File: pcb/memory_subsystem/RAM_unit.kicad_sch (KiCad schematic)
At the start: 6 parts, among them U3 74LS245

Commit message: Tracks finished
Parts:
- C1, C2, C3: footprint Capacitor_SMD:C_0805_2012Metric -> Capacitor_SMD:C_0805_2012Metric_Pad1.18x1.45mm_HandSolder
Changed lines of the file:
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@@
 			)
 		)
-		(property "Footprint" "Capacitor_SMD:C_0805_2012Metric"
+		(property "Footprint" "Capacitor_SMD:C_0805_2012Metric_Pad1.18x1.45mm_HandSolder"
 			(at 187.96 88.5952 0)
 			(hide yes)
@@
 			)
 		)
-		(property "Footprint" "Capacitor_SMD:C_0805_2012Metric"
+		(property "Footprint" "Capacitor_SMD:C_0805_2012Metric_Pad1.18x1.45mm_HandSolder"
 			(at 149.86 47.9552 0)
 			(hide yes)
@@
 			)
 		)
-		(property "Footprint" "Capacitor_SMD:C_0805_2012Metric"
+		(property "Footprint" "Capacitor_SMD:C_0805_2012Metric_Pad1.18x1.45mm_HandSolder"
 			(at 78.74 47.9552 0)
 			(hide yes)

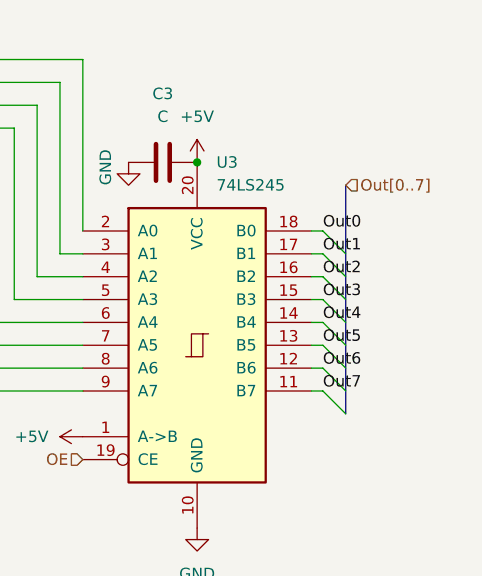
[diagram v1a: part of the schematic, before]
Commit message: Finished mem subsystem pcb
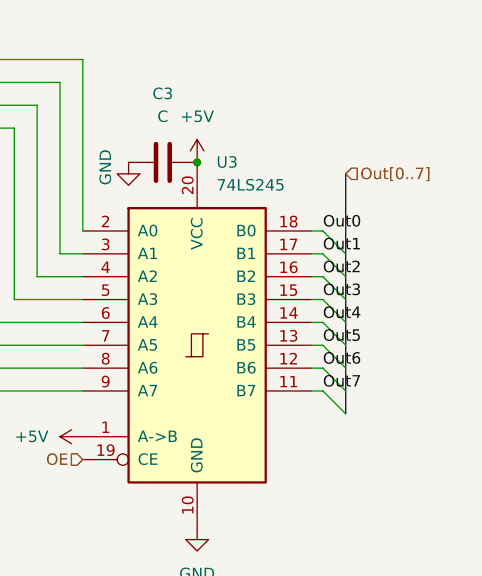
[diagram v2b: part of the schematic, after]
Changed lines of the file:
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@@
 	(bus
 		(pts
-			(xy 212.09 90.17) (xy 212.09 115.57)
+			(xy 212.09 88.9) (xy 212.09 115.57)
 		)
 		(stroke
@@
 	(hierarchical_label "Out[0..7]"
 		(shape input)
-		(at 212.09 90.17 0)
+		(at 212.09 88.9 0)
 		(effects
 			(font
@@
 					(unit 1)
 				)
+				(path "/eef9c2f8-b48e-448a-907d-9c9f187d4399/42f51e2d-d8b6-4a94-b1a8-da7d5a86e9c8"
+					(reference "#PWR038")
+					(unit 1)
+				)
 				(path "/eef9c2f8-b48e-448a-907d-9c9f187d4399/7681efea-75da-45e2-a65e-85a008f87d4d"
 					(reference "#PWR019")
-					(unit 1)
-				)
-				(path "/eef9c2f8-b48e-448a-907d-9c9f187d4399/ed633529-ad37-432a-9a64-2eb26cef90db"
-					(reference "#PWR039")
 					(unit 1)
 				)
@@
 					(unit 1)
 				)
+				(path "/eef9c2f8-b48e-448a-907d-9c9f187d4399/42f51e2d-d8b6-4a94-b1a8-da7d5a86e9c8"
+					(reference "#PWR040")
+					(unit 1)
+				)
 				(path "/eef9c2f8-b48e-448a-907d-9c9f187d4399/7681efea-75da-45e2-a65e-85a008f87d4d"
 					(reference "#PWR021")
-					(unit 1)
-				)
-				(path "/eef9c2f8-b48e-448a-907d-9c9f187d4399/ed633529-ad37-432a-9a64-2eb26cef90db"
-					(reference "#PWR041")
 					(unit 1)
 				)
@@
 					(unit 1)
 				)
+				(path "/eef9c2f8-b48e-448a-907d-9c9f187d4399/42f51e2d-d8b6-4a94-b1a8-da7d5a86e9c8"
+					(reference "#PWR037")
+					(unit 1)
+				)
 				(path "/eef9c2f8-b48e-448a-907d-9c9f187d4399/7681efea-75da-45e2-a65e-85a008f87d4d"
 					(reference "#PWR018")
-					(unit 1)
-				)
-				(path "/eef9c2f8-b48e-448a-907d-9c9f187d4399/ed633529-ad37-432a-9a64-2eb26cef90db"
-					(reference "#PWR038")
 					(unit 1)
 				)
@@
 					(unit 1)
 				)
+				(path "/eef9c2f8-b48e-448a-907d-9c9f187d4399/42f51e2d-d8b6-4a94-b1a8-da7d5a86e9c8"
+					(reference "C9")
+					(unit 1)
+				)
 				(path "/eef9c2f8-b48e-448a-907d-9c9f187d4399/7681efea-75da-45e2-a65e-85a008f87d4d"
 					(reference "C3")
-					(unit 1)
-				)
-				(path "/eef9c2f8-b48e-448a-907d-9c9f187d4399/ed633529-ad37-432a-9a64-2eb26cef90db"
-					(reference "C9")
 					(unit 1)
 				)
@@
 					(unit 1)
 				)
+				(path "/eef9c2f8-b48e-448a-907d-9c9f187d4399/42f51e2d-d8b6-4a94-b1a8-da7d5a86e9c8"
+					(reference "#PWR039")
+					(unit 1)
+				)
 				(path "/eef9c2f8-b48e-448a-907d-9c9f187d4399/7681efea-75da-45e2-a65e-85a008f87d4d"
 					(reference "#PWR020")
-					(unit 1)
-				)
-				(path "/eef9c2f8-b48e-448a-907d-9c9f187d4399/ed633529-ad37-432a-9a64-2eb26cef90db"
-					(reference "#PWR040")
 					(unit 1)
 				)
@@
 					(unit 1)
 				)
+				(path "/eef9c2f8-b48e-448a-907d-9c9f187d4399/42f51e2d-d8b6-4a94-b1a8-da7d5a86e9c8"
+					(reference "#PWR034")
+					(unit 1)
+				)
 				(path "/eef9c2f8-b48e-448a-907d-9c9f187d4399/7681efea-75da-45e2-a65e-85a008f87d4d"
 					(reference "#PWR015")
-					(unit 1)
-				)
-				(path "/eef9c2f8-b48e-448a-907d-9c9f187d4399/ed633529-ad37-432a-9a64-2eb26cef90db"
-					(reference "#PWR035")
 					(unit 1)
 				)
@@
 					(unit 1)
 				)
+				(path "/eef9c2f8-b48e-448a-907d-9c9f187d4399/42f51e2d-d8b6-4a94-b1a8-da7d5a86e9c8"
+					(reference "#PWR09")
+					(unit 1)
+				)
 				(path "/eef9c2f8-b48e-448a-907d-9c9f187d4399/7681efea-75da-45e2-a65e-85a008f87d4d"
 					(reference "#PWR013")
-					(unit 1)
-				)
-				(path "/eef9c2f8-b48e-448a-907d-9c9f187d4399/ed633529-ad37-432a-9a64-2eb26cef90db"
-					(reference "#PWR033")
 					(unit 1)
 				)
@@
 					(unit 1)
 				)
+				(path "/eef9c2f8-b48e-448a-907d-9c9f187d4399/42f51e2d-d8b6-4a94-b1a8-da7d5a86e9c8"
+					(reference "U9")
+					(unit 1)
+				)
 				(path "/eef9c2f8-b48e-448a-907d-9c9f187d4399/7681efea-75da-45e2-a65e-85a008f87d4d"
 					(reference "U3")
-					(unit 1)
-				)
-				(path "/eef9c2f8-b48e-448a-907d-9c9f187d4399/ed633529-ad37-432a-9a64-2eb26cef90db"
-					(reference "U9")
 					(unit 1)
 				)
@@
 					(unit 1)
 				)
+				(path "/eef9c2f8-b48e-448a-907d-9c9f187d4399/42f51e2d-d8b6-4a94-b1a8-da7d5a86e9c8"
+					(reference "#PWR041")
+					(unit 1)
+				)
 				(path "/eef9c2f8-b48e-448a-907d-9c9f187d4399/7681efea-75da-45e2-a65e-85a008f87d4d"
 					(reference "#PWR022")
-					(unit 1)
-				)
-				(path "/eef9c2f8-b48e-448a-907d-9c9f187d4399/ed633529-ad37-432a-9a64-2eb26cef90db"
-					(reference "#PWR042")
 					(unit 1)
 				)
@@
 					(unit 1)
 				)
+				(path "/eef9c2f8-b48e-448a-907d-9c9f187d4399/42f51e2d-d8b6-4a94-b1a8-da7d5a86e9c8"
+					(reference "U8")
+					(unit 1)
+				)
 				(path "/eef9c2f8-b48e-448a-907d-9c9f187d4399/7681efea-75da-45e2-a65e-85a008f87d4d"
 					(reference "U2")
-					(unit 1)
-				)
-				(path "/eef9c2f8-b48e-448a-907d-9c9f187d4399/ed633529-ad37-432a-9a64-2eb26cef90db"
-					(reference "U8")
 					(unit 1)
 				)
@@
 					(unit 1)
 				)
+				(path "/eef9c2f8-b48e-448a-907d-9c9f187d4399/42f51e2d-d8b6-4a94-b1a8-da7d5a86e9c8"
+					(reference "#PWR035")
+					(unit 1)
+				)
 				(path "/eef9c2f8-b48e-448a-907d-9c9f187d4399/7681efea-75da-45e2-a65e-85a008f87d4d"
 					(reference "#PWR016")
-					(unit 1)
-				)
-				(path "/eef9c2f8-b48e-448a-907d-9c9f187d4399/ed633529-ad37-432a-9a64-2eb26cef90db"
-					(reference "#PWR036")
 					(unit 1)
 				)
@@
 					(unit 1)
 				)
+				(path "/eef9c2f8-b48e-448a-907d-9c9f187d4399/42f51e2d-d8b6-4a94-b1a8-da7d5a86e9c8"
+					(reference "#PWR033")
+					(unit 1)
+				)
 				(path "/eef9c2f8-b48e-448a-907d-9c9f187d4399/7681efea-75da-45e2-a65e-85a008f87d4d"
 					(reference "#PWR014")
-					(unit 1)
-				)
-				(path "/eef9c2f8-b48e-448a-907d-9c9f187d4399/ed633529-ad37-432a-9a64-2eb26cef90db"
-					(reference "#PWR034")
 					(unit 1)
 				)
@@
 					(unit 1)
 				)
+				(path "/eef9c2f8-b48e-448a-907d-9c9f187d4399/42f51e2d-d8b6-4a94-b1a8-da7d5a86e9c8"
+					(reference "C8")
+					(unit 1)
+				)
 				(path "/eef9c2f8-b48e-448a-907d-9c9f187d4399/7681efea-75da-45e2-a65e-85a008f87d4d"
 					(reference "C2")
-					(unit 1)
-				)
-				(path "/eef9c2f8-b48e-448a-907d-9c9f187d4399/ed633529-ad37-432a-9a64-2eb26cef90db"
-					(reference "C8")
 					(unit 1)
 				)
@@
 					(unit 1)
 				)
+				(path "/eef9c2f8-b48e-448a-907d-9c9f187d4399/42f51e2d-d8b6-4a94-b1a8-da7d5a86e9c8"
+					(reference "#PWR036")
+					(unit 1)
+				)
 				(path "/eef9c2f8-b48e-448a-907d-9c9f187d4399/7681efea-75da-45e2-a65e-85a008f87d4d"
 					(reference "#PWR017")
-					(unit 1)
-				)
-				(path "/eef9c2f8-b48e-448a-907d-9c9f187d4399/ed633529-ad37-432a-9a64-2eb26cef90db"
-					(reference "#PWR037")
 					(unit 1)
 				)
@@
 					(unit 1)
 				)
+				(path "/eef9c2f8-b48e-448a-907d-9c9f187d4399/42f51e2d-d8b6-4a94-b1a8-da7d5a86e9c8"
+					(reference "C7")
+					(unit 1)
+				)
 				(path "/eef9c2f8-b48e-448a-907d-9c9f187d4399/7681efea-75da-45e2-a65e-85a008f87d4d"
 					(reference "C1")
-					(unit 1)
-				)
-				(path "/eef9c2f8-b48e-448a-907d-9c9f187d4399/ed633529-ad37-432a-9a64-2eb26cef90db"
-					(reference "C7")
 					(unit 1)
 				)
@@
 					(unit 1)
 				)
+				(path "/eef9c2f8-b48e-448a-907d-9c9f187d4399/42f51e2d-d8b6-4a94-b1a8-da7d5a86e9c8"
+					(reference "U7")
+					(unit 1)
+				)
 				(path "/eef9c2f8-b48e-448a-907d-9c9f187d4399/7681efea-75da-45e2-a65e-85a008f87d4d"
 					(reference "U1")
 					(unit 1)
 				)
-				(path "/eef9c2f8-b48e-448a-907d-9c9f187d4399/ed633529-ad37-432a-9a64-2eb26cef90db"
-					(reference "U7")
-					(unit 1)
-				)
